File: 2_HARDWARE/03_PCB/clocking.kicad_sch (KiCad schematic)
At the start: 23 parts, among them U10 LMK1C1103PWR, U9 ADG1219BRJZ, X1 ASE-10.000MHz, X2 ASE-100.000MHz

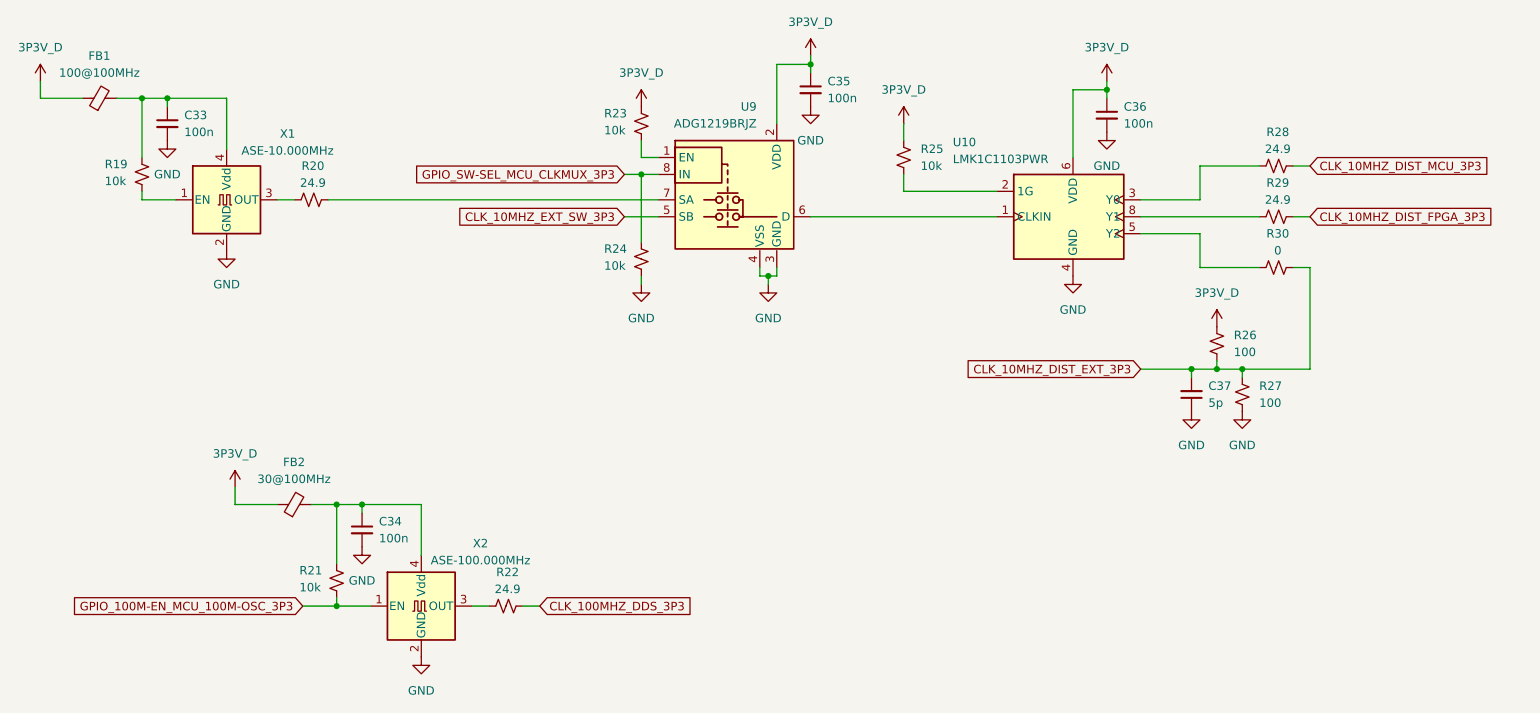
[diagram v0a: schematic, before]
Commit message: MINOR: Changed Boot Select Switches to Pull-Downs / Pull Up DNI and continued layout.
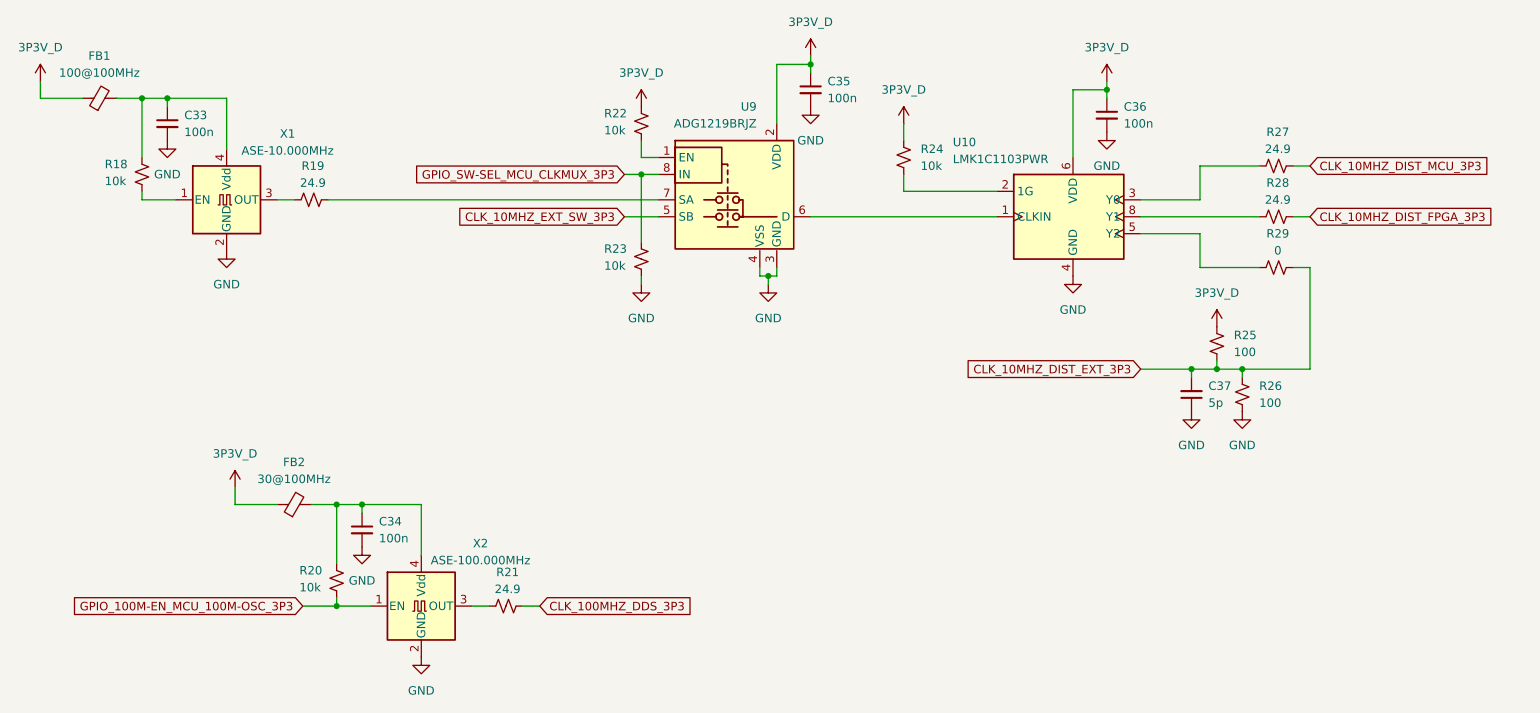
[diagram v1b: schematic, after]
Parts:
- renumbered R19 to R18, R20 to R19, R21 to R20, R22 to R21, R23 to R22, R24 to R23, R25 to R24, R26 to R25, R27 to R26, R28 to R27, R29 to R28, R30 to R29
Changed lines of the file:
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@@
 		(on_board yes)
 		(dnp no)
-		(property "Reference" "R29"
+		(property "Reference" "R28"
 			(at 216.154 92.71 90)
 			(effects
@@
 			(project "arb"
 				(path "/866ef9be-3b01-4288-a6e0-a2357aa17e50/59503b16-13c4-4480-8e22-c5a7043d8844"
-					(reference "R29")
+					(reference "R28")
 					(unit 1)
 				)
@@
 		(dnp no)
 		(fields_autoplaced yes)
-		(property "Reference" "#PWR073"
+		(property "Reference" "#PWR071"
 			(at 49.53 92.71 0)
 			(effects
@@
 			(project "arb"
 				(path "/866ef9be-3b01-4288-a6e0-a2357aa17e50/59503b16-13c4-4480-8e22-c5a7043d8844"
-					(reference "#PWR073")
+					(reference "#PWR071")
 					(unit 1)
 				)
@@
 		(dnp no)
 		(fields_autoplaced yes)
-		(property "Reference" "#PWR085"
+		(property "Reference" "#PWR083"
 			(at 190.5 81.28 0)
 			(effects
@@
 			(project "arb"
 				(path "/866ef9be-3b01-4288-a6e0-a2357aa17e50/59503b16-13c4-4480-8e22-c5a7043d8844"
-					(reference "#PWR085")
+					(reference "#PWR083")
 					(unit 1)
 				)
@@
 		(dnp no)
 		(fields_autoplaced yes)
-		(property "Reference" "#PWR078"
+		(property "Reference" "#PWR076"
 			(at 120.65 85.09 0)
 			(effects
@@
 			(project "arb"
 				(path "/866ef9be-3b01-4288-a6e0-a2357aa17e50/59503b16-13c4-4480-8e22-c5a7043d8844"
-					(reference "#PWR078")
+					(reference "#PWR076")
 					(unit 1)
 				)
@@
 		(dnp no)
 		(fields_autoplaced yes)
-		(property "Reference" "#PWR074"
+		(property "Reference" "#PWR072"
 			(at 58.42 109.22 0)
 			(effects
@@
 			(project "arb"
 				(path "/866ef9be-3b01-4288-a6e0-a2357aa17e50/59503b16-13c4-4480-8e22-c5a7043d8844"
-					(reference "#PWR074")
+					(reference "#PWR072")
 					(unit 1)
 				)
@@
 		(dnp no)
 		(fields_autoplaced yes)
-		(property "Reference" "#PWR088"
+		(property "Reference" "#PWR086"
 			(at 207.01 118.11 0)
 			(effects
@@
 			(project "arb"
 				(path "/866ef9be-3b01-4288-a6e0-a2357aa17e50/59503b16-13c4-4480-8e22-c5a7043d8844"
-					(reference "#PWR088")
+					(reference "#PWR086")
 					(unit 1)
 				)
@@
 		(dnp no)
 		(fields_autoplaced yes)
-		(property "Reference" "#PWR087"
+		(property "Reference" "#PWR085"
 			(at 203.2 133.35 0)
 			(effects
@@
 			(project "arb"
 				(path "/866ef9be-3b01-4288-a6e0-a2357aa17e50/59503b16-13c4-4480-8e22-c5a7043d8844"
-					(reference "#PWR087")
+					(reference "#PWR085")
 					(unit 1)
 				)
@@
 		(dnp no)
 		(fields_autoplaced yes)
-		(property "Reference" "#PWR076"
+		(property "Reference" "#PWR074"
 			(at 78.74 153.67 0)
 			(effects
@@
 			(project "arb"
 				(path "/866ef9be-3b01-4288-a6e0-a2357aa17e50/59503b16-13c4-4480-8e22-c5a7043d8844"
-					(reference "#PWR076")
+					(reference "#PWR074")
 					(unit 1)
 				)
@@
 		(on_board yes)
 		(dnp no)
-		(property "Reference" "R24"
+		(property "Reference" "R23"
 			(at 115.062 102.616 0)
 			(effects
@@
 			(project "arb"
 				(path "/866ef9be-3b01-4288-a6e0-a2357aa17e50/59503b16-13c4-4480-8e22-c5a7043d8844"
-					(reference "R24")
+					(reference "R23")
 					(unit 1)
 				)
@@
 		(dnp no)
 		(fields_autoplaced yes)
-		(property "Reference" "#PWR089"
+		(property "Reference" "#PWR087"
 			(at 210.82 133.35 0)
 			(effects
@@
 			(project "arb"
 				(path "/866ef9be-3b01-4288-a6e0-a2357aa17e50/59503b16-13c4-4480-8e22-c5a7043d8844"
-					(reference "#PWR089")
+					(reference "#PWR087")
 					(unit 1)
 				)
@@
 		(on_board yes)
 		(dnp no)
-		(property "Reference" "R20"
+		(property "Reference" "R19"
 			(at 71.374 90.17 90)
 			(effects
@@
 			(project "arb"
 				(path "/866ef9be-3b01-4288-a6e0-a2357aa17e50/59503b16-13c4-4480-8e22-c5a7043d8844"
-					(reference "R20")
+					(reference "R19")
 					(unit 1)
 				)
@@
 		(dnp no)
 		(fields_autoplaced yes)
-		(property "Reference" "#PWR084"
+		(property "Reference" "#PWR082"
 			(at 185.42 113.03 0)
 			(effects
@@
 			(project "arb"
 				(path "/866ef9be-3b01-4288-a6e0-a2357aa17e50/59503b16-13c4-4480-8e22-c5a7043d8844"
-					(reference "#PWR084")
+					(reference "#PWR082")
 					(unit 1)
 				)
@@
 		(dnp no)
 		(fields_autoplaced yes)
-		(property "Reference" "R27"
+		(property "Reference" "R26"
 			(at 213.36 123.1899 0)
 			(effects
@@
 			(project "arb"
 				(path "/866ef9be-3b01-4288-a6e0-a2357aa17e50/59503b16-13c4-4480-8e22-c5a7043d8844"
-					(reference "R27")
+					(reference "R26")
 					(unit 1)
 				)
@@
 		(dnp no)
 		(fields_autoplaced yes)
-		(property "Reference" "#PWR080"
+		(property "Reference" "#PWR078"
 			(at 139.7 114.3 0)
 			(effects
@@
 			(project "arb"
 				(path "/866ef9be-3b01-4288-a6e0-a2357aa17e50/59503b16-13c4-4480-8e22-c5a7043d8844"
-					(reference "#PWR080")
+					(reference "#PWR078")
 					(unit 1)
 				)
@@
 		(dnp no)
 		(fields_autoplaced yes)
-		(property "Reference" "R25"
+		(property "Reference" "R24"
 			(at 162.56 87.6299 0)
 			(effects
@@
 			(project "arb"
 				(path "/866ef9be-3b01-4288-a6e0-a2357aa17e50/59503b16-13c4-4480-8e22-c5a7043d8844"
-					(reference "R25")
+					(reference "R24")
 					(unit 1)
 				)
@@
 		(dnp no)
 		(fields_autoplaced yes)
-		(property "Reference" "#PWR079"
+		(property "Reference" "#PWR077"
 			(at 120.65 114.3 0)
 			(effects
@@
 			(project "arb"
 				(path "/866ef9be-3b01-4288-a6e0-a2357aa17e50/59503b16-13c4-4480-8e22-c5a7043d8844"
-					(reference "#PWR079")
+					(reference "#PWR077")
 					(unit 1)
 				)
@@
 		(dnp no)
 		(fields_autoplaced yes)
-		(property "Reference" "#PWR077"
+		(property "Reference" "#PWR075"
 			(at 87.63 170.18 0)
 			(effects
@@
 			(project "arb"
 				(path "/866ef9be-3b01-4288-a6e0-a2357aa17e50/59503b16-13c4-4480-8e22-c5a7043d8844"
-					(reference "#PWR077")
+					(reference "#PWR075")
 					(unit 1)
 				)
@@
 		(dnp no)
 		(fields_autoplaced yes)
-		(property "Reference" "#PWR075"
+		(property "Reference" "#PWR073"
 			(at 59.69 142.24 0)
 			(effects
@@
 			(project "arb"
 				(path "/866ef9be-3b01-4288-a6e0-a2357aa17e50/59503b16-13c4-4480-8e22-c5a7043d8844"
-					(reference "#PWR075")
+					(reference "#PWR073")
 					(unit 1)
 				)
@@
 		(on_board yes)
 		(dnp no)
-		(property "Reference" "R21"
+		(property "Reference" "R20"
 			(at 69.342 150.876 0)
 			(effects
@@
 			(project "arb"
 				(path "/866ef9be-3b01-4288-a6e0-a2357aa17e50/59503b16-13c4-4480-8e22-c5a7043d8844"
-					(reference "R21")
+					(reference "R20")
 					(unit 1)
 				)
@@
 		(dnp no)
 		(fields_autoplaced yes)
-		(property "Reference" "#PWR083"
+		(property "Reference" "#PWR081"
 			(at 160.02 87.63 0)
 			(effects
@@
 			(project "arb"
 				(path "/866ef9be-3b01-4288-a6e0-a2357aa17e50/59503b16-13c4-4480-8e22-c5a7043d8844"
-					(reference "#PWR083")
+					(reference "#PWR081")
 					(unit 1)
 				)
@@
 		(dnp no)
 		(fields_autoplaced yes)
-		(property "Reference" "#PWR081"
+		(property "Reference" "#PWR079"
 			(at 146.05 77.47 0)
 			(effects
@@
 			(project "arb"
 				(path "/866ef9be-3b01-4288-a6e0-a2357aa17e50/59503b16-13c4-4480-8e22-c5a7043d8844"
-					(reference "#PWR081")
+					(reference "#PWR079")
 					(unit 1)
 				)
@@
 		(on_board yes)
 		(dnp no)
-		(property "Reference" "R22"
+		(property "Reference" "R21"
 			(at 100.584 151.13 90)
 			(effects
@@
 			(project "arb"
 				(path "/866ef9be-3b01-4288-a6e0-a2357aa17e50/59503b16-13c4-4480-8e22-c5a7043d8844"
-					(reference "R22")
+					(reference "R21")
 					(unit 1)
 				)
@@
 		(dnp no)
 		(fields_autoplaced yes)
-		(property "Reference" "#PWR086"
+		(property "Reference" "#PWR084"
 			(at 190.5 91.44 0)
 			(effects
@@
 			(project "arb"
 				(path "/866ef9be-3b01-4288-a6e0-a2357aa17e50/59503b16-13c4-4480-8e22-c5a7043d8844"
-					(reference "#PWR086")
+					(reference "#PWR084")
 					(unit 1)
 				)
@@
 		(on_board yes)
 		(dnp no)
-		(property "Reference" "R30"
+		(property "Reference" "R29"
 			(at 216.154 100.33 90)
 			(effects
@@
 			(project "arb"
 				(path "/866ef9be-3b01-4288-a6e0-a2357aa17e50/59503b16-13c4-4480-8e22-c5a7043d8844"
-					(reference "R30")
+					(reference "R29")
 					(unit 1)
 				)
@@
 		(on_board yes)
 		(dnp no)
-		(property "Reference" "R23"
+		(property "Reference" "R22"
 			(at 115.062 82.296 0)
 			(effects
@@
 			(project "arb"
 				(path "/866ef9be-3b01-4288-a6e0-a2357aa17e50/59503b16-13c4-4480-8e22-c5a7043d8844"
-					(reference "R23")
+					(reference "R22")
 					(unit 1)
 				)
@@
 		(on_board yes)
 		(dnp no)
-		(property "Reference" "R19"
+		(property "Reference" "R18"
 			(at 40.132 89.916 0)
 			(effects
@@
 			(project "arb"
 				(path "/866ef9be-3b01-4288-a6e0-a2357aa17e50/59503b16-13c4-4480-8e22-c5a7043d8844"
-					(reference "R19")
+					(reference "R18")
 					(unit 1)
 				)
@@
 		(on_board yes)
 		(dnp no)
-		(property "Reference" "R28"
+		(property "Reference" "R27"
 			(at 216.154 85.09 90)
 			(effects
@@
 			(project "arb"
 				(path "/866ef9be-3b01-4288-a6e0-a2357aa17e50/59503b16-13c4-4480-8e22-c5a7043d8844"
-					(reference "R28")
+					(reference "R27")
 					(unit 1)
 				)
@@
 		(dnp no)
 		(fields_autoplaced yes)
-		(property "Reference" "R26"
+		(property "Reference" "R25"
 			(at 209.55 115.5699 0)
 			(effects
@@
 			(project "arb"
 				(path "/866ef9be-3b01-4288-a6e0-a2357aa17e50/59503b16-13c4-4480-8e22-c5a7043d8844"
-					(reference "R26")
+					(reference "R25")
 					(unit 1)
 				)
@@
 		(dnp no)
 		(fields_autoplaced yes)
-		(property "Reference" "#PWR082"
+		(property "Reference" "#PWR080"
 			(at 146.05 87.63 0)
 			(effects
@@
 			(project "arb"
 				(path "/866ef9be-3b01-4288-a6e0-a2357aa17e50/59503b16-13c4-4480-8e22-c5a7043d8844"
-					(reference "#PWR082")
+					(reference "#PWR080")
 					(unit 1)
 				)
@@
 		(dnp no)
 		(fields_autoplaced yes)
-		(property "Reference" "#PWR072"
+		(property "Reference" "#PWR070"
 			(at 30.48 81.28 0)
 			(effects
@@
 			(project "arb"
 				(path "/866ef9be-3b01-4288-a6e0-a2357aa17e50/59503b16-13c4-4480-8e22-c5a7043d8844"
-					(reference "#PWR072")
-					(unit 1)
-				)
+					(reference "#PWR070")
+					(unit 1)
+				)
